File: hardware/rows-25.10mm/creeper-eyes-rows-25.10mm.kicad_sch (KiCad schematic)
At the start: 5 parts, among them J3 OLED, Frank's right eye, J4 OLED, Frank's left eye, J5 DS3231 RTC (optional), U1 ESP32 DevKit V1 (30 pin)

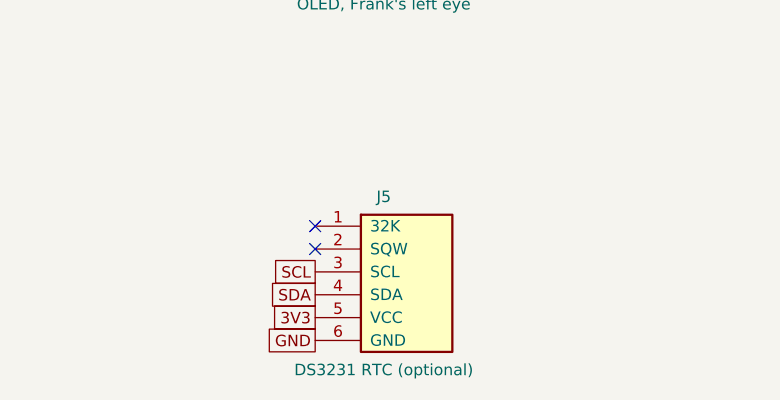
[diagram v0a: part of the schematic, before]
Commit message: Rev B: an RTC header the DS3231 mini plugs onto
Rev A's J5 followed the six-pin ZS-042 (32K SQW SCL SDA VCC GND).  The
module actually in use is the five-pin DS3231 mini sold for the
Raspberry Pi, labelled + D C NC -, which needed jumpers.

J5 is now five pins on rows 12-16, VCC SDA SCL NC GND from the top, GND
on the bottom pin.  SCL keeps its route; SDA comes down its column to
row 13 rather than 15, which avoids the row-14 GND run it would
otherwise have to cross; VCC and GND take rows 12 and 16.  Rows 14-18
were tried first and failed DRC on the bottom-right mounting hole.

ERC clean, schematic and board netlists agree on all 51 nodes, DRC
clean, for both row pitches.  Gerbers regenerated.  The hardware README
gains a Revisions section, with the jumper wiring for rev A boards.

Co-Authored-By: Claude Opus 5.5 <noreply@anthropic.com>
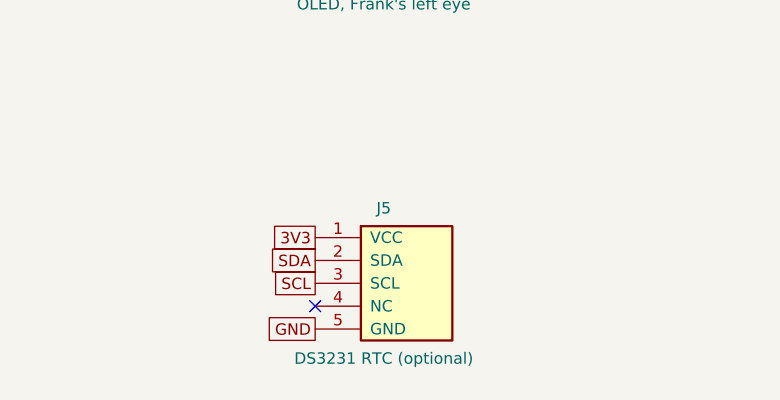
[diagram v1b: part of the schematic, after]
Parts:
- J5: footprint Connector_PinHeader_2.54mm:PinHeader_1x06_P2.54mm_Vertical -> Connector_PinHeader_2.54mm:PinHeader_1x05_P2.54mm_Vertical
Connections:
- net 3V3: now also J5.1 (VCC); no longer J5.5 (VCC)
- net GND: now also J5.5 (GND); no longer J5.6 (GND)
- net SDA: now also J5.2 (SDA); no longer J5.4 (SDA)
- no-connect marks 21 -> 20
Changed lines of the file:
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@@
 		(at 60.96 148.59 0)
 		(unit 1) (body_style 1) (exclude_from_sim no) (in_bom yes) (on_board yes) (dnp no)
-		(property "Reference" "J5" (at 60.96 138.97 0) (effects (font (size 1.27 1.27))))
-		(property "Value" "DS3231 RTC (optional)" (at 60.96 158.21 0) (effects (font (size 1.27 1.27))))
-		(property "Footprint" "Connector_PinHeader_2.54mm:PinHeader_1x06_P2.54mm_Vertical" (at 60.96 148.59 0) (effects (font (size 1.27 1.27)) (hide yes)))
+		(property "Reference" "J5" (at 60.96 140.24 0) (effects (font (size 1.27 1.27))))
+		(property "Value" "DS3231 RTC (optional)" (at 60.96 156.94 0) (effects (font (size 1.27 1.27))))
+		(property "Footprint" "Connector_PinHeader_2.54mm:PinHeader_1x05_P2.54mm_Vertical" (at 60.96 148.59 0) (effects (font (size 1.27 1.27)) (hide yes)))
 		(property "Datasheet" "" (at 60.96 148.59 0) (effects (font (size 1.27 1.27)) (hide yes)))
 		(property "Description" "" (at 60.96 148.59 0) (effects (font (size 1.27 1.27)) (hide yes)))
@@
 		(pin "4")
 		(pin "5")
-		(pin "6")
 		(instances (project "creeper-eyes-rows-25.10mm" (path "/3c0ffee0-5eed-4c0d-b0a7-c0ffee000001" (reference "J5") (unit 1))))
 	)
-	(no_connect (at 53.34 142.24))
-	(no_connect (at 53.34 144.78))
-	(global_label "SCL" (shape passive) (at 53.34 147.32 180) (fields_autoplaced yes)
+	(global_label "3V3" (shape passive) (at 53.34 143.51 180) (fields_autoplaced yes)
 		(effects (font (size 1.27 1.27)) (justify right))
-		(property "Intersheetrefs" "${INTERSHEET_REFS}" (at 53.34 147.32 0)
+		(property "Intersheetrefs" "${INTERSHEET_REFS}" (at 53.34 143.51 0)
 			(effects (font (size 1.27 1.27)) (justify right) (hide yes)))
 	)
-	(global_label "SDA" (shape passive) (at 53.34 149.86 180) (fields_autoplaced yes)
+	(global_label "SDA" (shape passive) (at 53.34 146.05 180) (fields_autoplaced yes)
 		(effects (font (size 1.27 1.27)) (justify right))
-		(property "Intersheetrefs" "${INTERSHEET_REFS}" (at 53.34 149.86 0)
+		(property "Intersheetrefs" "${INTERSHEET_REFS}" (at 53.34 146.05 0)
 			(effects (font (size 1.27 1.27)) (justify right) (hide yes)))
 	)
-	(global_label "3V3" (shape passive) (at 53.34 152.4 180) (fields_autoplaced yes)
+	(global_label "SCL" (shape passive) (at 53.34 148.59 180) (fields_autoplaced yes)
 		(effects (font (size 1.27 1.27)) (justify right))
-		(property "Intersheetrefs" "${INTERSHEET_REFS}" (at 53.34 152.4 0)
+		(property "Intersheetrefs" "${INTERSHEET_REFS}" (at 53.34 148.59 0)
 			(effects (font (size 1.27 1.27)) (justify right) (hide yes)))
 	)
-	(global_label "GND" (shape passive) (at 53.34 154.94 180) (fields_autoplaced yes)
+	(no_connect (at 53.34 151.13))
+	(global_label "GND" (shape passive) (at 53.34 153.67 180) (fields_autoplaced yes)
 		(effects (font (size 1.27 1.27)) (justify right))
-		(property "Intersheetrefs" "${INTERSHEET_REFS}" (at 53.34 154.94 0)
+		(property "Intersheetrefs" "${INTERSHEET_REFS}" (at 53.34 153.67 0)
 			(effects (font (size 1.27 1.27)) (justify right) (hide yes)))
 	)
